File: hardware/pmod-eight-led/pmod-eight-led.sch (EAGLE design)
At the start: 19 parts, among them J1 PMOD_PLUG1

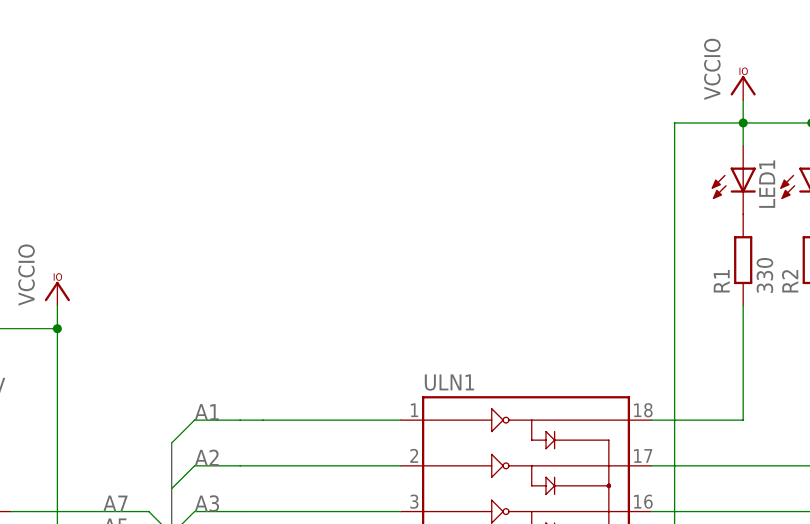
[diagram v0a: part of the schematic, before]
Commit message: Updated led pmod
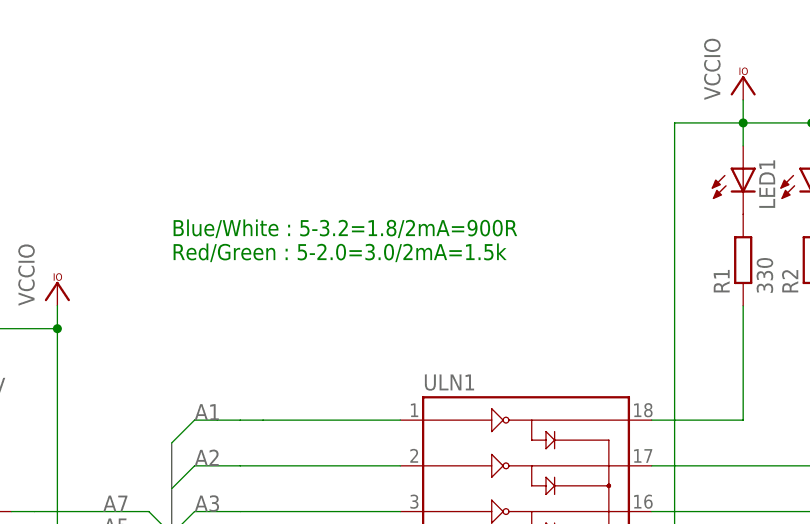
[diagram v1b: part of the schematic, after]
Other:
- note added: "Blue/White : 5-3.2=1.8/2mA=900R Red/Green : 5-2.0=3.0/2mA=1.5k"
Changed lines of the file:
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@@
 <grid distance="0.1" unitdist="inch" unit="inch" style="lines" multiple="1" display="no" altdistance="0.01" altunitdist="inch" altunit="inch"/>
 <layers>
-<layer number="1" name="Top" color="4" fill="1" visible="yes" active="no"/>
-<layer number="16" name="Bottom" color="1" fill="1" visible="yes" active="no"/>
-<layer number="17" name="Pads" color="2" fill="1" visible="yes" active="no"/>
-<layer number="18" name="Vias" color="2" fill="1" visible="yes" active="no"/>
-<layer number="19" name="Unrouted" color="6" fill="1" visible="yes" active="no"/>
-<layer number="20" name="Dimension" color="15" fill="1" visible="yes" active="no"/>
-<layer number="21" name="tPlace" color="7" fill="1" visible="yes" active="no"/>
-<layer number="22" name="bPlace" color="7" fill="1" visible="yes" active="no"/>
-<layer number="23" name="tOrigins" color="15" fill="1" visible="yes" active="no"/>
-<layer number="24" name="bOrigins" color="15" fill="1" visible="yes" active="no"/>
-<layer number="25" name="tNames" color="7" fill="1" visible="yes" active="no"/>
-<layer number="26" name="bNames" color="7" fill="1" visible="yes" active="no"/>
-<layer number="27" name="tValues" color="7" fill="1" visible="yes" active="no"/>
-<layer number="28" name="bValues" color="7" fill="1" visible="yes" active="no"/>
+<layer number="1" name="Top" color="4" fill="1" visible="no" active="no"/>
+<layer number="16" name="Bottom" color="1" fill="1" visible="no" active="no"/>
+<layer number="17" name="Pads" color="2" fill="1" visible="no" active="no"/>
+<layer number="18" name="Vias" color="2" fill="1" visible="no" active="no"/>
+<layer number="19" name="Unrouted" color="6" fill="1" visible="no" active="no"/>
+<layer number="20" name="Dimension" color="15" fill="1" visible="no" active="no"/>
+<layer number="21" name="tPlace" color="7" fill="1" visible="no" active="no"/>
+<layer number="22" name="bPlace" color="7" fill="1" visible="no" active="no"/>
+<layer number="23" name="tOrigins" color="15" fill="1" visible="no" active="no"/>
+<layer number="24" name="bOrigins" color="15" fill="1" visible="no" active="no"/>
+<layer number="25" name="tNames" color="7" fill="1" visible="no" active="no"/>
+<layer number="26" name="bNames" color="7" fill="1" visible="no" active="no"/>
+<layer number="27" name="tValues" color="7" fill="1" visible="no" active="no"/>
+<layer number="28" name="bValues" color="7" fill="1" visible="no" active="no"/>
 <layer number="29" name="tStop" color="7" fill="3" visible="no" active="no"/>
 <layer number="30" name="bStop" color="7" fill="6" visible="no" active="no"/>
@@
 <layer number="35" name="tGlue" color="7" fill="4" visible="no" active="no"/>
 <layer number="36" name="bGlue" color="7" fill="5" visible="no" active="no"/>
-<layer number="37" name="tTest" color="7" fill="1" visible="yes" active="no"/>
-<layer number="38" name="bTest" color="7" fill="1" visible="yes" active="no"/>
+<layer number="37" name="tTest" color="7" fill="1" visible="no" active="no"/>
+<layer number="38" name="bTest" color="7" fill="1" visible="no" active="no"/>
 <layer number="39" name="tKeepout" color="4" fill="11" visible="no" active="no"/>
 <layer number="40" name="bKeepout" color="1" fill="11" visible="no" active="no"/>
@@
 <layer number="44" name="Drills" color="7" fill="1" visible="no" active="no"/>
 <layer number="45" name="Holes" color="7" fill="1" visible="no" active="no"/>
-<layer number="46" name="Milling" color="3" fill="1" visible="yes" active="no"/>
-<layer number="47" name="Measures" color="7" fill="1" visible="yes" active="no"/>
-<layer number="48" name="Document" color="7" fill="1" visible="yes" active="no"/>
-<layer number="49" name="Reference" color="7" fill="1" visible="yes" active="no"/>
-<layer number="50" name="dxf" color="7" fill="1" visible="yes" active="no"/>
-<layer number="51" name="tDocu" color="7" fill="1" visible="yes" active="no"/>
-<layer number="52" name="bDocu" color="7" fill="1" visible="yes" active="no"/>
-<layer number="53" name="tGND_GNDA" color="7" fill="1" visible="yes" active="no"/>
-<layer number="54" name="bGND_GNDA" color="7" fill="1" visible="yes" active="no"/>
-<layer number="56" name="wert" color="7" fill="1" visible="yes" active="no"/>
-<layer number="57" name="tCAD" color="7" fill="1" visible="yes" active="no"/>
-<layer number="59" name="tCarbon" color="7" fill="1" visible="yes" active="no"/>
-<layer number="60" name="bCarbon" color="7" fill="1" visible="yes" active="no"/>
+<layer number="46" name="Milling" color="3" fill="1" visible="no" active="no"/>
+<layer number="47" name="Measures" color="7" fill="1" visible="no" active="no"/>
+<layer number="48" name="Document" color="7" fill="1" visible="no" active="no"/>
+<layer number="49" name="Reference" color="7" fill="1" visible="no" active="no"/>
+<layer number="50" name="dxf" color="7" fill="1" visible="no" active="no"/>
+<layer number="51" name="tDocu" color="7" fill="1" visible="no" active="no"/>
+<layer number="52" name="bDocu" color="7" fill="1" visible="no" active="no"/>
+<layer number="53" name="tGND_GNDA" color="7" fill="1" visible="no" active="no"/>
+<layer number="54" name="bGND_GNDA" color="7" fill="1" visible="no" active="no"/>
+<layer number="56" name="wert" color="7" fill="1" visible="no" active="no"/>
+<layer number="57" name="tCAD" color="7" fill="1" visible="no" active="no"/>
+<layer number="59" name="tCarbon" color="7" fill="1" visible="no" active="no"/>
+<layer number="60" name="bCarbon" color="7" fill="1" visible="no" active="no"/>
 <layer number="88" name="SimResults" color="9" fill="1" visible="yes" active="yes"/>
 <layer number="89" name="SimProbes" color="9" fill="1" visible="yes" active="yes"/>
@@
 <sheet>
 <plain>
+<text x="12.7" y="33.02" size="1.778" layer="91">Blue/White : 5-3.2=1.8/2mA=900R
+Red/Green : 5-2.0=3.0/2mA=1.5k</text>
 </plain>
 <instances>
@@
 </schematic>
 </drawing>
+<compatibility>
+<note version="6.3" minversion="6.2.2" severity="warning">
+Since Version 6.2.2 text objects can contain more than one line,
+which will not be processed correctly with this version.
+</note>
+</compatibility>
 </eagle>
